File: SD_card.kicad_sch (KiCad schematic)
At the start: 8 parts

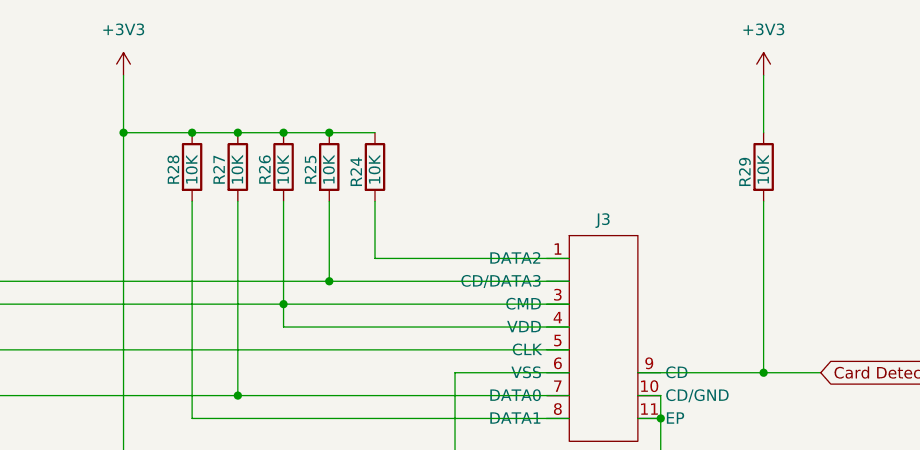
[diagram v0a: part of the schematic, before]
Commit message: schematic for stm32u545
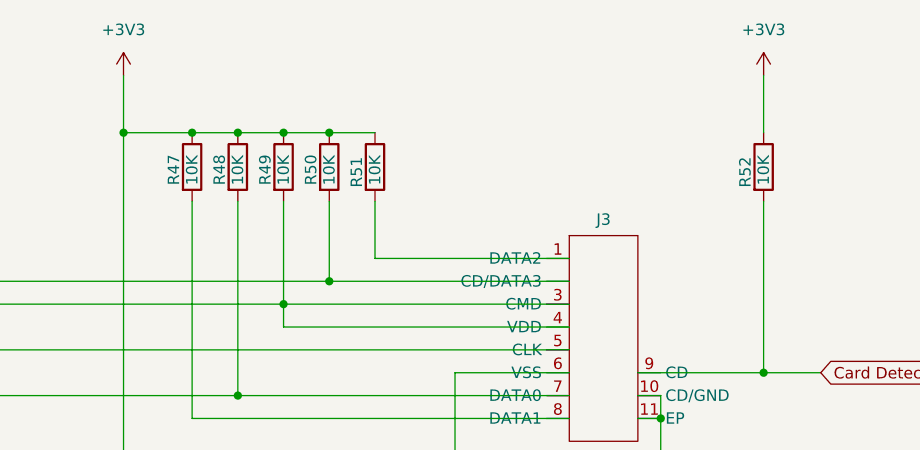
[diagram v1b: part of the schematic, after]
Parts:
- renumbered R28 to R47, R27 to R48, R26 to R49, R25 to R50, R24 to R51, R29 to R52
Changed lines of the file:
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@@
 		(on_board yes)
 		(dnp no)
-		(property "Reference" "R28"
+		(property "Reference" "R47"
 			(at 110.998 85.852 90)
 			(effects
@@
 			(project "TDT4295"
 				(path "/071102f3-276b-4b6b-8738-8c534a30b197/91cac871-d497-4887-ab60-4a820d2ee1af"
-					(reference "R28")
+					(reference "R47")
 					(unit 1)
 				)
@@
 		(on_board yes)
 		(dnp no)
-		(property "Reference" "R29"
+		(property "Reference" "R52"
 			(at 174.498 86.106 90)
 			(effects
@@
 			(project "TDT4295"
 				(path "/071102f3-276b-4b6b-8738-8c534a30b197/91cac871-d497-4887-ab60-4a820d2ee1af"
-					(reference "R29")
+					(reference "R52")
 					(unit 1)
 				)
@@
 		(on_board yes)
 		(dnp no)
-		(property "Reference" "R27"
+		(property "Reference" "R48"
 			(at 116.078 85.852 90)
 			(effects
@@
 			(project "TDT4295"
 				(path "/071102f3-276b-4b6b-8738-8c534a30b197/91cac871-d497-4887-ab60-4a820d2ee1af"
-					(reference "R27")
+					(reference "R48")
 					(unit 1)
 				)
@@
 		(on_board yes)
 		(dnp no)
-		(property "Reference" "R24"
+		(property "Reference" "R51"
 			(at 131.318 86.106 90)
 			(effects
@@
 			(project ""
 				(path "/071102f3-276b-4b6b-8738-8c534a30b197/91cac871-d497-4887-ab60-4a820d2ee1af"
-					(reference "R24")
+					(reference "R51")
 					(unit 1)
 				)
@@
 		(on_board yes)
 		(dnp no)
-		(property "Reference" "R25"
+		(property "Reference" "R50"
 			(at 126.238 85.852 90)
 			(effects
@@
 			(project "TDT4295"
 				(path "/071102f3-276b-4b6b-8738-8c534a30b197/91cac871-d497-4887-ab60-4a820d2ee1af"
-					(reference "R25")
+					(reference "R50")
 					(unit 1)
 				)
@@
 		(on_board yes)
 		(dnp no)
-		(property "Reference" "R26"
+		(property "Reference" "R49"
 			(at 121.158 85.852 90)
 			(effects
@@
 			(project "TDT4295"
 				(path "/071102f3-276b-4b6b-8738-8c534a30b197/91cac871-d497-4887-ab60-4a820d2ee1af"
-					(reference "R26")
-					(unit 1)
-				)
+					(reference "R49")
+					(unit 1)
+				)

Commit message: updated footprints
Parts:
- R47, R48, R49, R50, R51, R52: footprint (none) -> Resistor_SMD:R_0805_2012Metric
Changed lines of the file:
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@@
 			)
 		)
-		(property "Footprint" ""
+		(property "Footprint" "Resistor_SMD:R_0805_2012Metric"
 			(at 111.252 83.82 90)
 			(effects
@@
 			)
 		)
-		(property "Footprint" ""
+		(property "Footprint" "Resistor_SMD:R_0805_2012Metric"
 			(at 174.752 83.82 90)
 			(effects
@@
 			)
 		)
-		(property "Footprint" ""
+		(property "Footprint" "Resistor_SMD:R_0805_2012Metric"
 			(at 116.332 83.82 90)
 			(effects
@@
 			)
 		)
-		(property "Footprint" ""
+		(property "Footprint" "Resistor_SMD:R_0805_2012Metric"
 			(at 131.572 83.82 90)
 			(effects
@@
 			)
 		)
-		(property "Footprint" ""
+		(property "Footprint" "Resistor_SMD:R_0805_2012Metric"
 			(at 126.492 83.82 90)
 			(effects
@@
 			)
 		)
-		(property "Footprint" ""
+		(property "Footprint" "Resistor_SMD:R_0805_2012Metric"
 			(at 121.412 83.82 90)
 			(effects
